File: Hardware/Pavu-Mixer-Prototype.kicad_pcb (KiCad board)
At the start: 2 copper layers, 155.9 x 91.9 mm, 65 parts, among them J1 Conn_02x16_Counter_Clockwise, U1 74HC595, U2 74HC595, U3 74HC595, U4 PCA9555D, U5 PCA9536D

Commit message: Import AISLER design rules
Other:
- net class Default: clearance 0.2 -> 0.25
- net class Min added: clearance 0.1, trace_width 0.1, via_dia 0.45, via_drill 0.2
- rule trace_clearance: 0.2 -> 0.25
- rule trace_min: 0.2 -> 0.1
- rule via_min_drill: 0.3 -> 0.2
- rule via_min_size: 0.4 -> 0.45

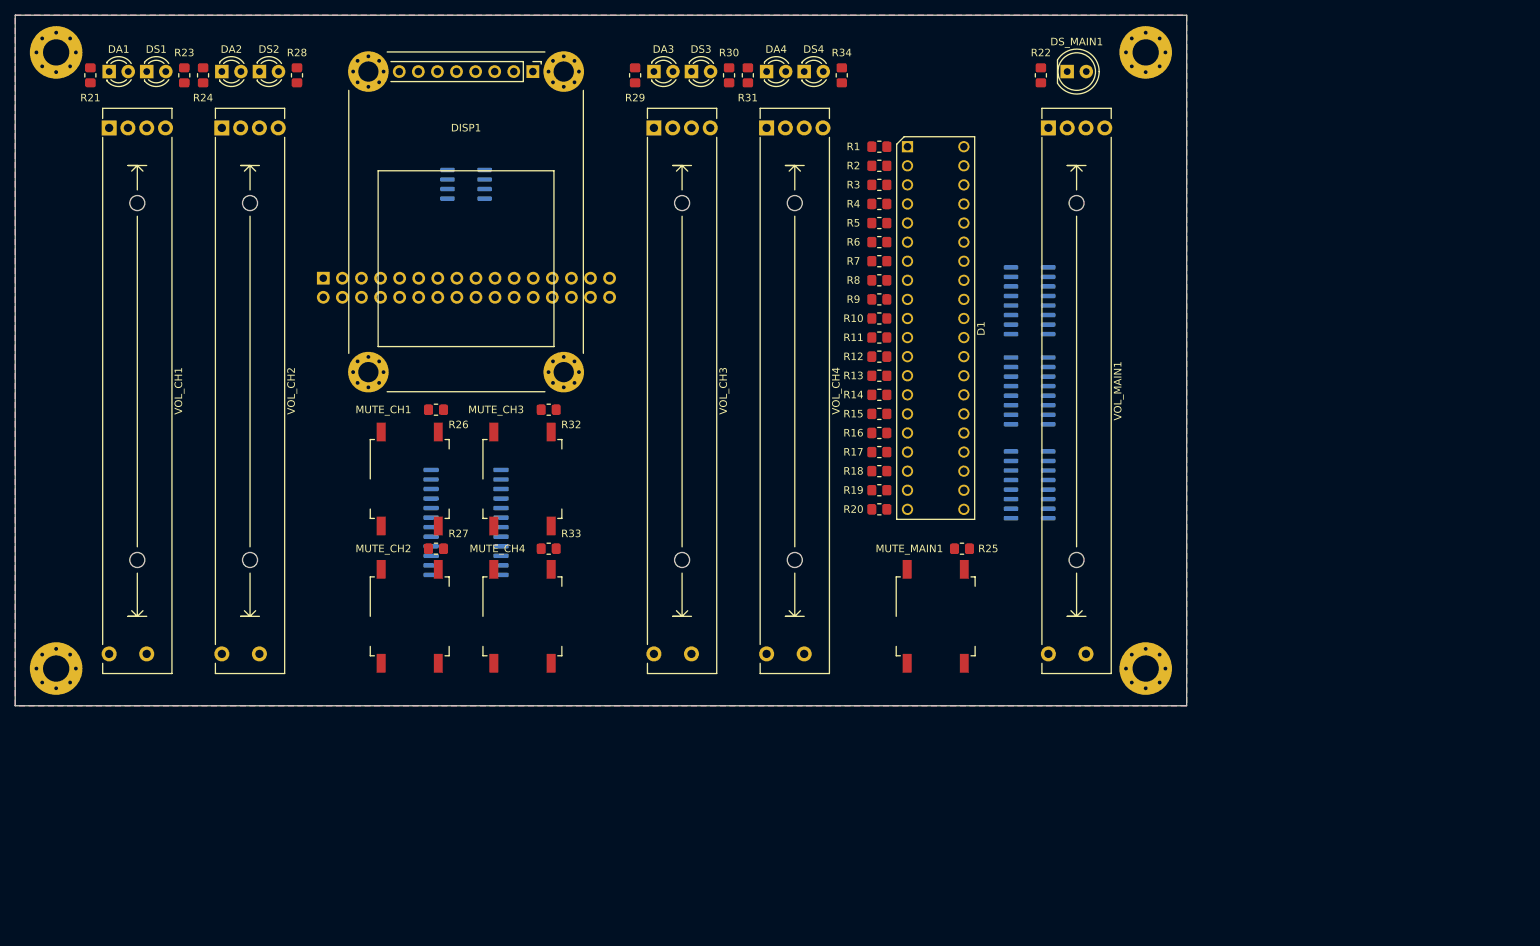
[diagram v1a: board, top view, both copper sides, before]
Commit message: Center the board on the sheet
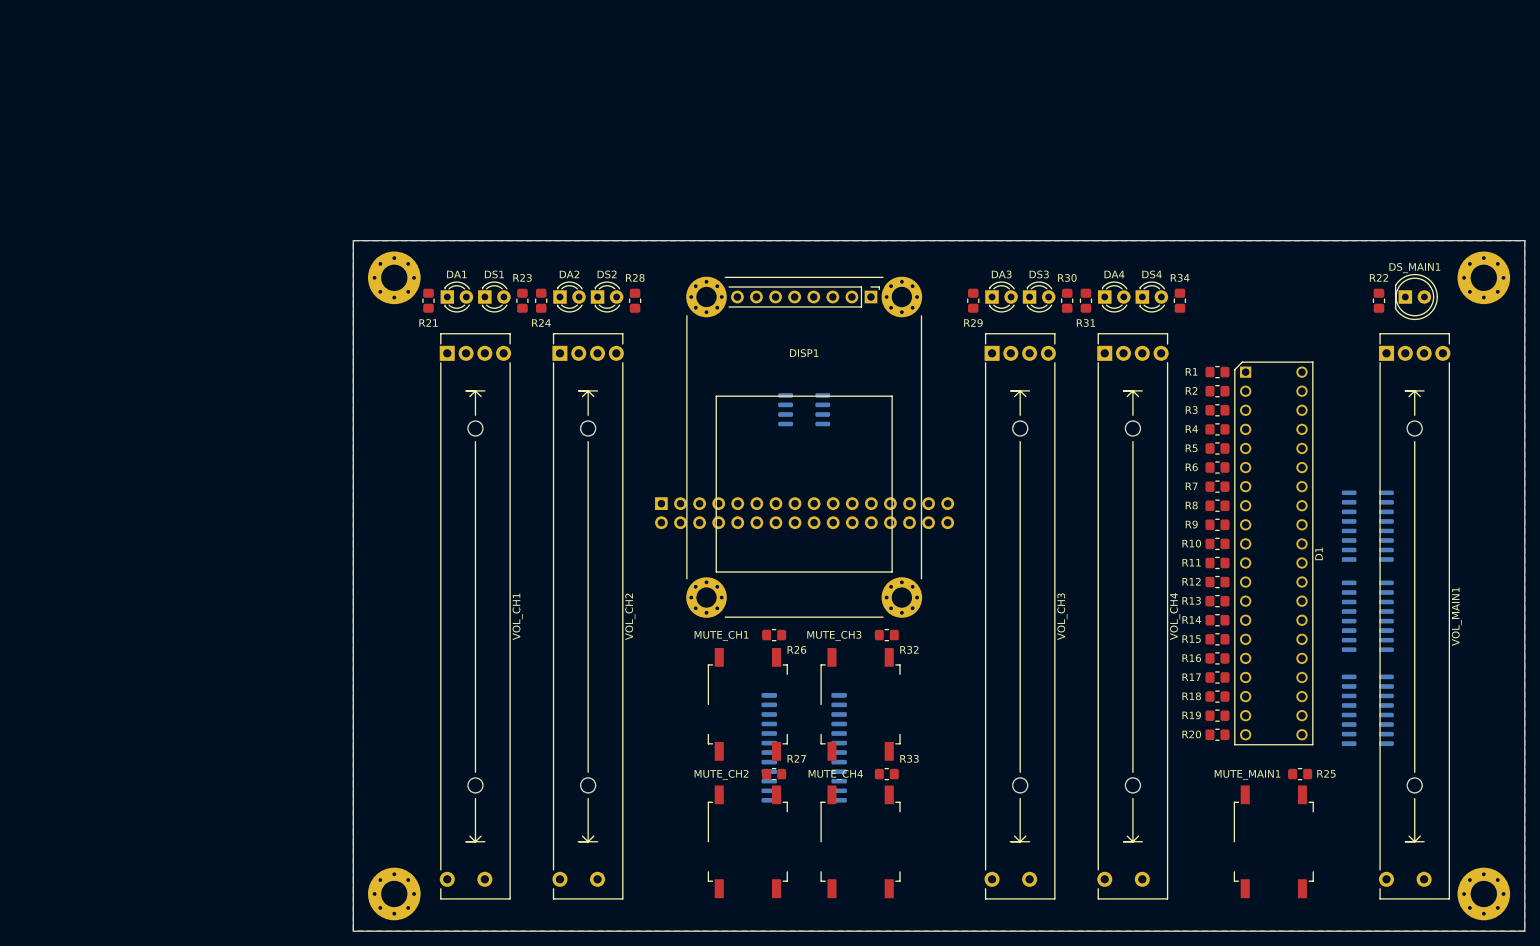
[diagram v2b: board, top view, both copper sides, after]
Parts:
- moved D1 54.1 mm to (188.8, 72.5)
- moved DA1 54.1 mm to (82.5, 62.5)
- moved DA2 54.1 mm to (97.5, 62.5)
- moved DA3 54.1 mm to (155.0, 62.5)
- moved DA4 54.1 mm to (170.0, 62.5)
- moved DISP1 54.1 mm to (130.0, 62.5)
- moved DS1 54.1 mm to (87.5, 62.5)
- moved DS2 54.1 mm to (102.5, 62.5)
- moved DS3 54.1 mm to (160.0, 62.5)
- moved DS4 54.1 mm to (175.0, 62.5)
- moved DS_MAIN1 54.1 mm to (210.0, 62.5)
- moved H1 54.1 mm to (75.5, 60.0)
- moved H3 54.1 mm to (220.4, 60.0)
- moved J1 54.1 mm to (111.0, 90.0)
- moved MUTE_CH1 54.1 mm to (122.5, 116.7)
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
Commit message: Fully routed layout
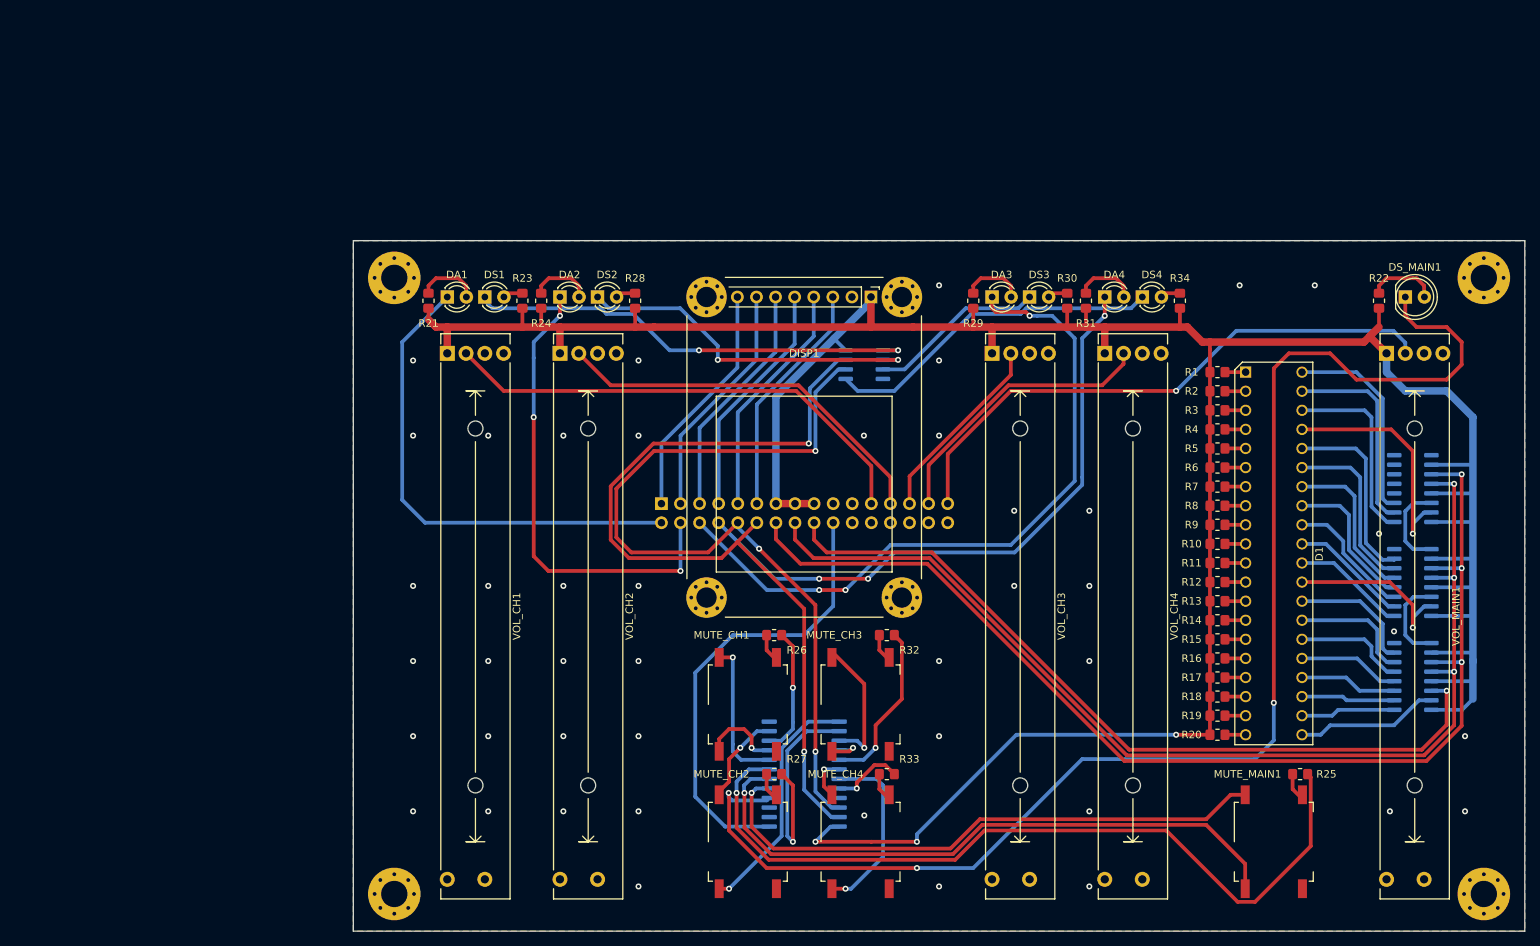
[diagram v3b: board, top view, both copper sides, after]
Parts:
- moved U5 10.0 mm to (138.0, 71.5), turned to 180 degrees
- moved U1 7.81 mm to (211.0, 88.0)
- moved U2 7.50 mm to (211.0, 100.5)
- moved U3 7.50 mm to (211.0, 113.0)
- moved U4 3.50 mm to (130.0, 126.0)
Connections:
- J1 pad 14: MAINVOL_RCLK -> MAINVOL_SRCLK
- J1 pad 16: MAINVOL_SRCLK -> MAINVOL_RCLK
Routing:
- net +3V3: track 0.00 -> 430.3 mm, vias 0 -> 3
- net /DESYNC_MAIN: track 0.00 -> 185.0 mm, vias 0 -> 3
- net MAINVOL_SRCLK: track 0.00 -> 153.3 mm, vias 0 -> 3
- net MAINVOL_RCLK: track 0.00 -> 144.9 mm, vias 0 -> 3
- net I2C_SDA: track 0.00 -> 114.9 mm, vias 0 -> 2
- net I2C_SCL: track 0.00 -> 110.5 mm, vias 0 -> 3
- net /MUTE_MAIN_LED2: track 0.00 -> 107.7 mm, vias 0 -> 1
- net MAINVOL_SER: track 0.00 -> 106.0 mm, vias 0 -> 1
- net VOL3: track 0.00 -> 92.8 mm, vias 0 -> 3
- net /MUTE_MAIN_LED1: track 0.00 -> 84.6 mm, vias 0 -> 1
- net VOL4: track 0.00 -> 82.9 mm, vias 0 -> 3
- net /MUTE_MAIN_BTN: track 0.00 -> 76.9 mm, vias 0 -> 1
- net MAIN: track 0.00 -> 76.4 mm, vias 0 -> 1
- net VOL1: track 0.00 -> 65.2 mm
- net CH1: track 0.00 -> 65.2 mm
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
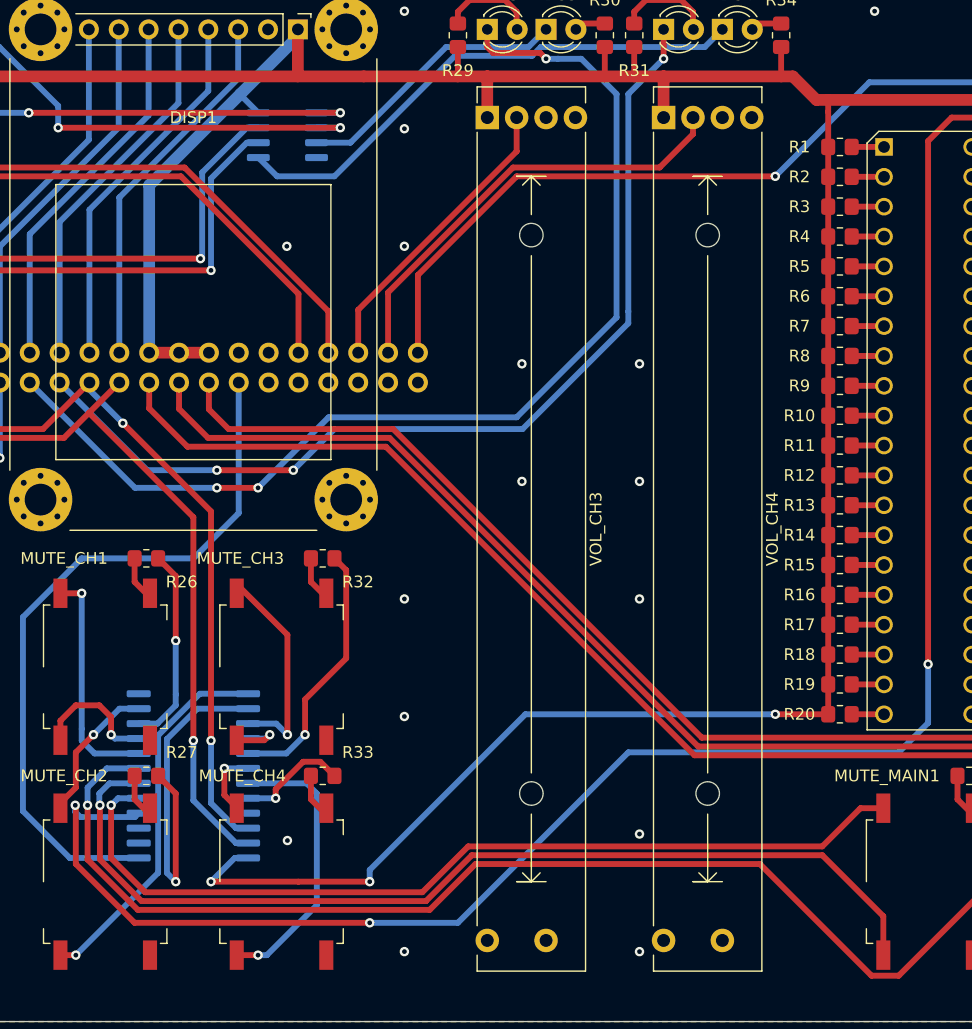
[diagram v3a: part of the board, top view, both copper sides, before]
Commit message: Minor routing improvements
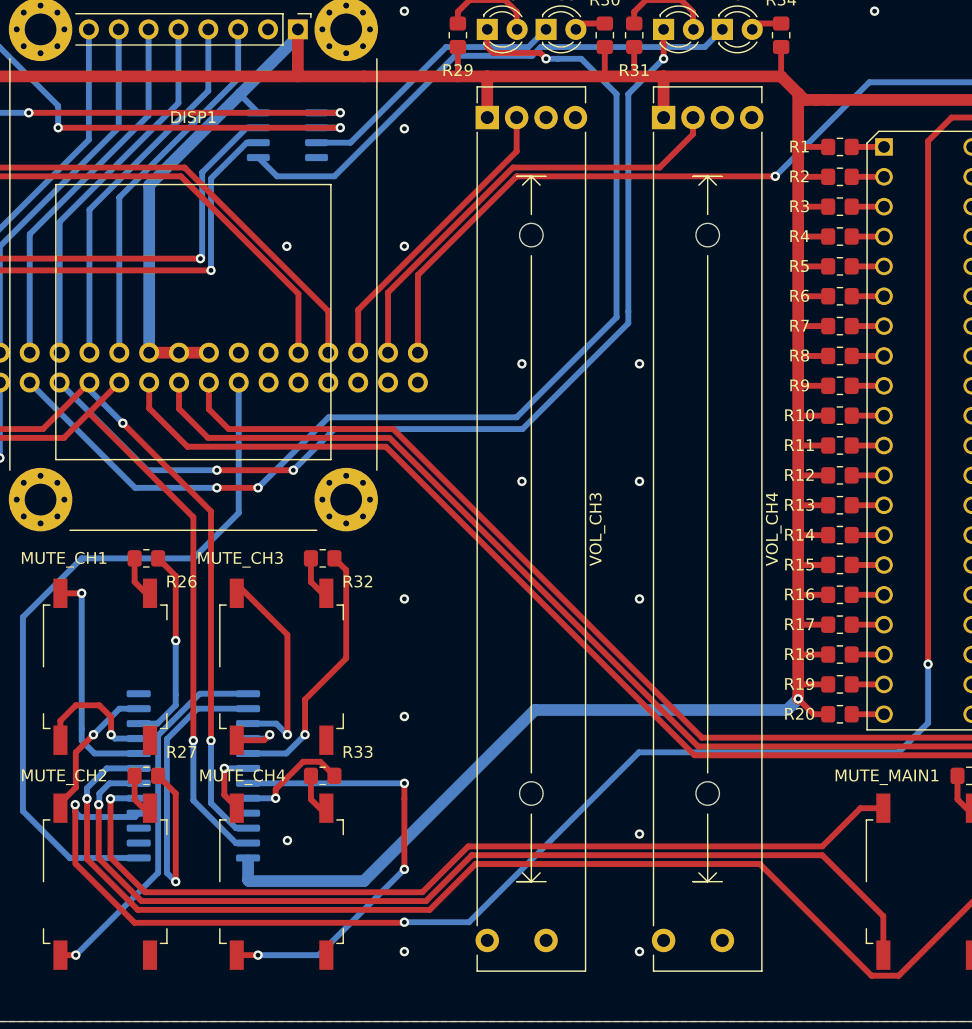
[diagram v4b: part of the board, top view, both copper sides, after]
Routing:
- net +3V3: track 430.3 -> 473.3 mm, vias 3 -> 1
- net /MUTE4_LED1: track 24.3 -> 37.9 mm, vias 1 -> 3
